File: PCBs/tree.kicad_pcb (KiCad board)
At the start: 2 copper layers, 31 parts, among them J1 Conn_01x06_Female, SW1 SW_Push_DPDT, SW2 SW_SPST, U1 Shift_Reg, U2 Shift_Reg, U3 Shift_Reg, U4 pic18f45k20

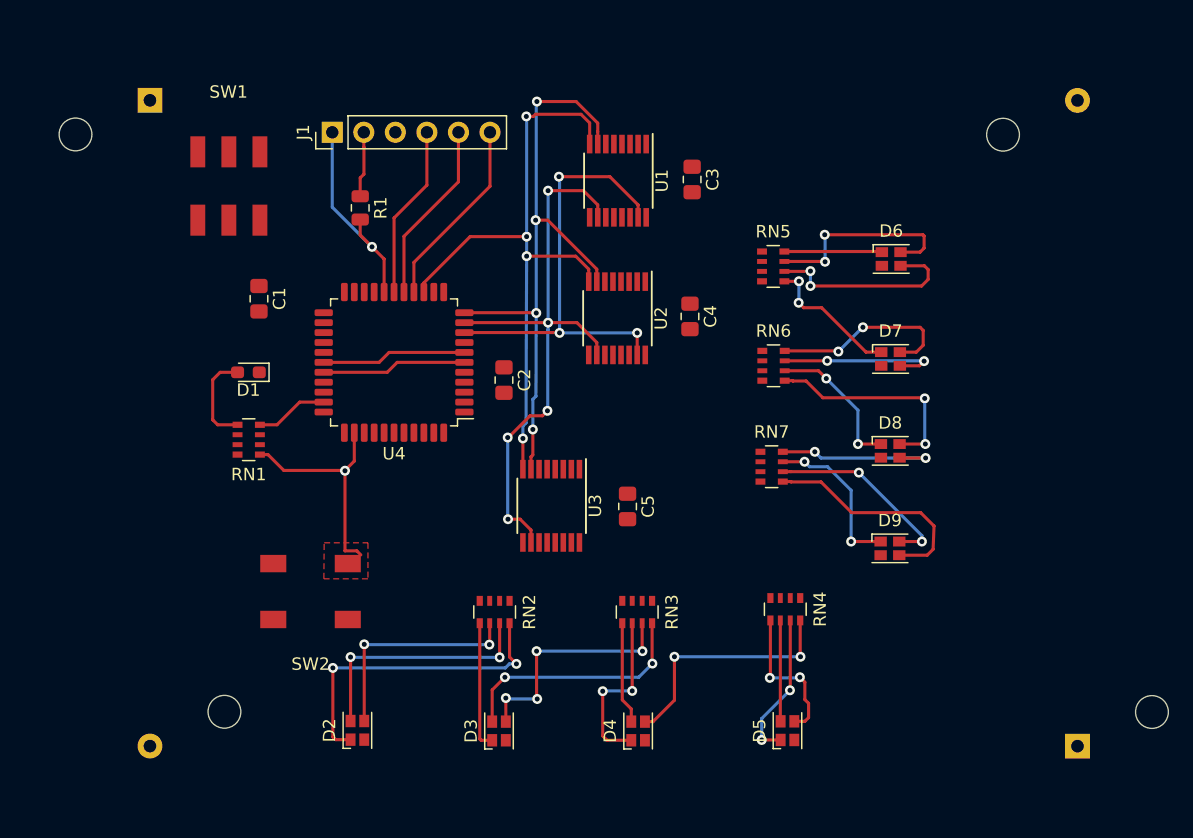
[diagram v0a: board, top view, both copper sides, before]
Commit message: Finished Bulk of routing. Reformated traces to use 6/6 mils as per board house rules.
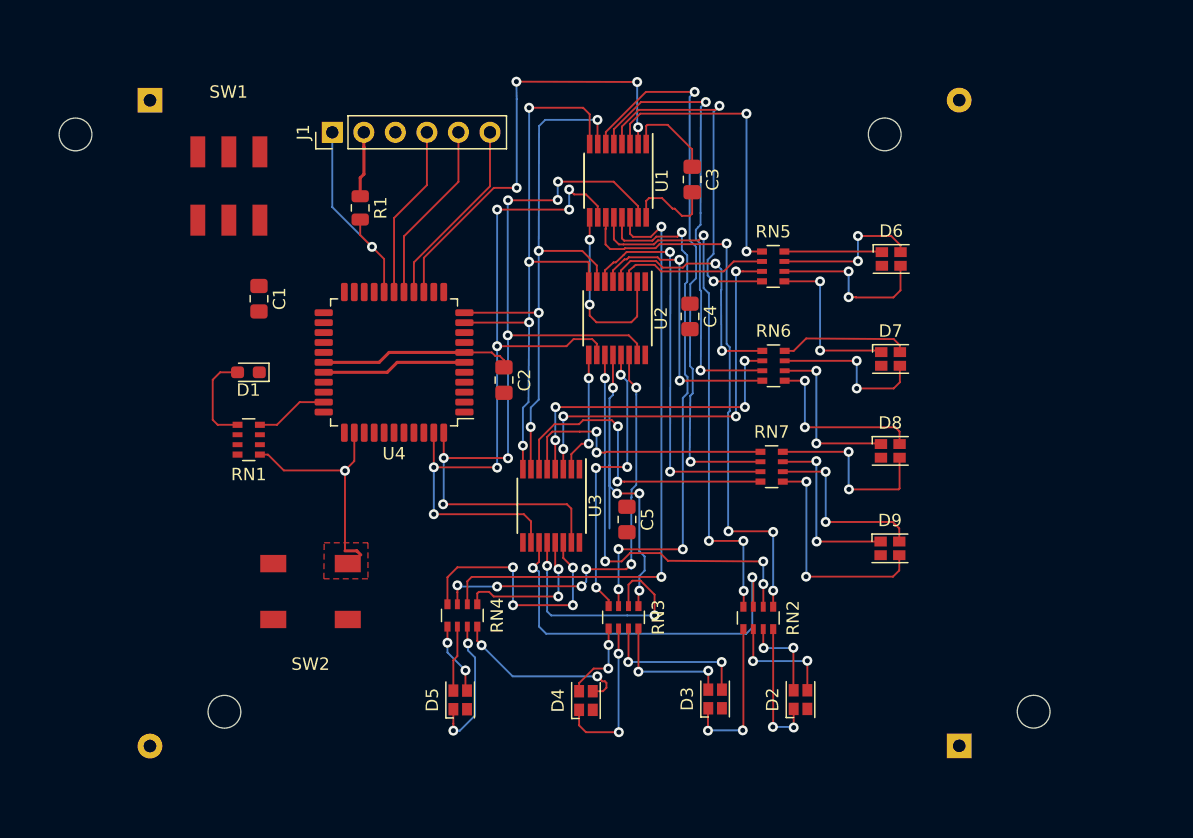
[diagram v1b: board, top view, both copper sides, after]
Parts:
- moved D2 35.8 mm to (212.1, 122.7)
- moved D5 26.5 mm to (184.7, 122.7)
- moved RN4 26.0 mm to (184.8, 115.9)
- moved RN2 21.2 mm to (208.7, 116.1)
- moved D3 17.6 mm to (205.2, 122.6)
- moved BT2 9.53 mm to (224.8, 126.4)
- moved D4 4.86 mm to (194.8, 122.7)
- moved RN3 1.18 mm to (197.8, 116.0)
- moved C5 1.05 mm to (198.1, 108.2)
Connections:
- U4 pad 10: Storage_CLK -> ~Output_Enable~
- U4 pad 14: ~Output_Enable~ -> Red_Data
- U4 pad 43: Net-(U4-Pad43) -> Storage_CLK
- U4 pad 44: Net-(U4-Pad44) -> Shift_CLK
- U4 pad 8: Red_Data -> Net-(U4-Pad8)
- U4 pad 9: Shift_CLK -> Net-(U4-Pad9)
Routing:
- net R8: track 0.00 -> 50.1 mm, vias 0 -> 2
- net R4: track 0.00 -> 46.1 mm, vias 0 -> 2
- net R5: track 0.00 -> 45.3 mm, vias 0 -> 4
- net R7: track 0.00 -> 42.7 mm, vias 0 -> 4
- net R6: track 0.00 -> 42.3 mm, vias 0 -> 4
- net R3: track 0.00 -> 36.6 mm, vias 0 -> 2
- net Red_Data: track 0.00 -> 35.9 mm, vias 0 -> 4
- net G8: track 0.00 -> 34.6 mm, vias 0 -> 6
- net Shift_CLK: track 36.6 -> 70.2 mm, vias 3 -> 7
- net G5: track 0.00 -> 33.5 mm, vias 0 -> 4
- net B1: track 0.00 -> 31.9 mm, vias 0 -> 4
- net G4: track 0.00 -> 31.7 mm, vias 0 -> 2
- net B5: track 0.00 -> 31.3 mm, vias 0 -> 2
- net R2: track 0.00 -> 28.6 mm, vias 0 -> 2
- net G6: track 0.00 -> 27.9 mm, vias 0 -> 4
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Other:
- net class Default: clearance 0.2 -> 0.1524; trace_width 0.25 -> 0.1524
- rule trace_clearance: 0.2 -> 0.1524
- rule trace_min: 0.2 -> 0.1524

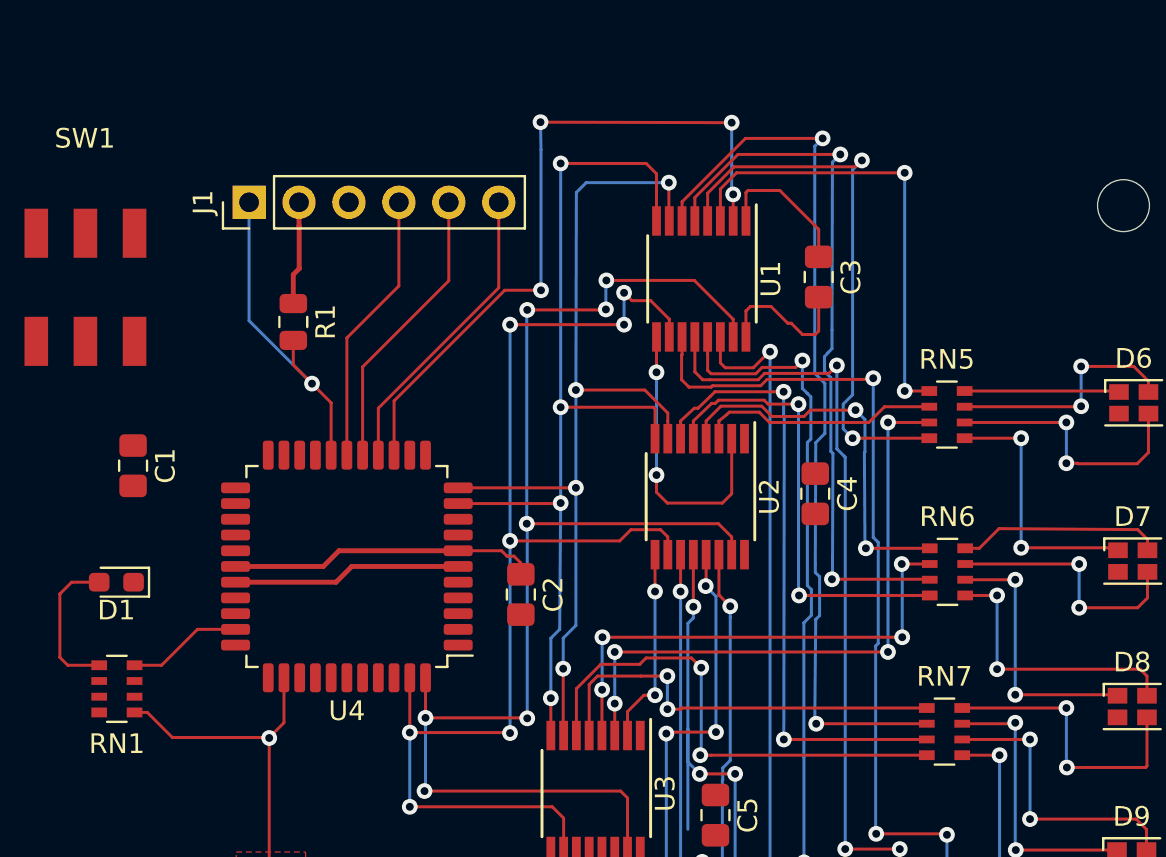
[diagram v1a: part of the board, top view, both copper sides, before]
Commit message: Laid out a board with debug header and LPC804
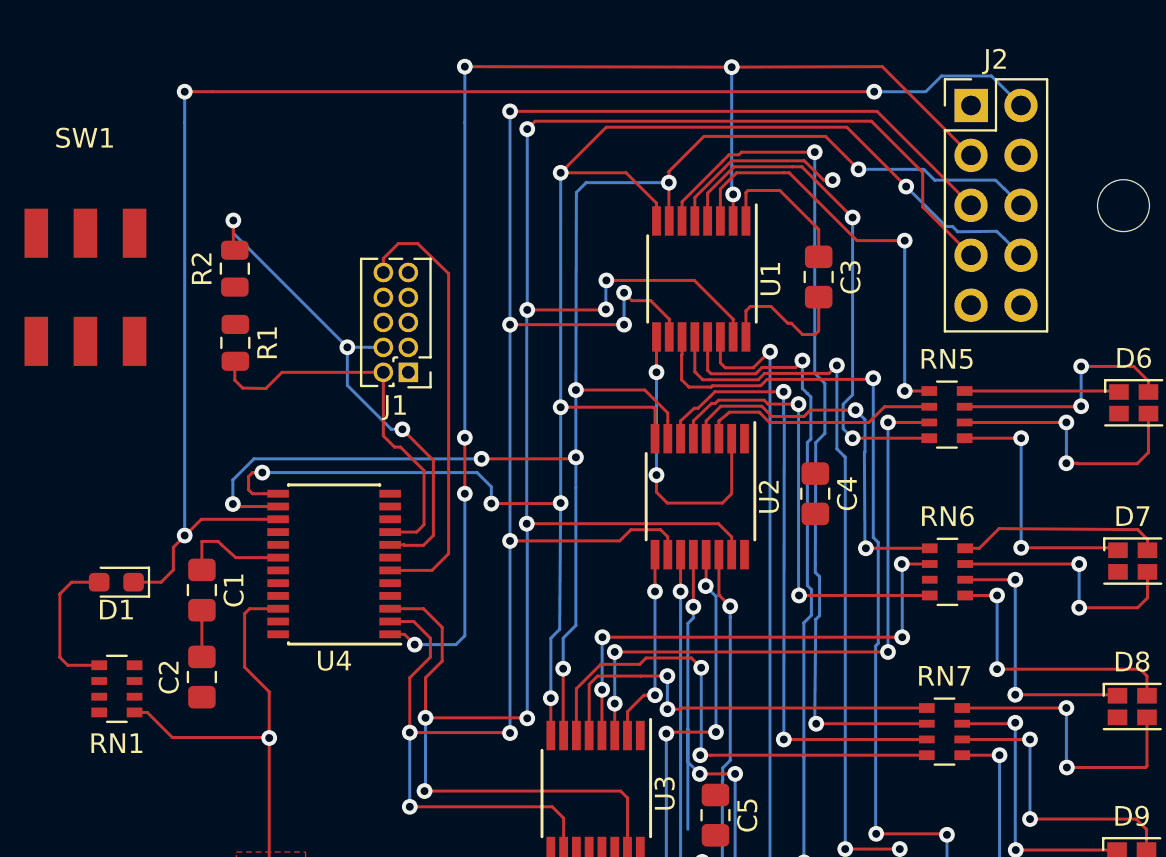
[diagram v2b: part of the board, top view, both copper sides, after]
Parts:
- added J2: Conn_02x05_Odd_Even, Connector_PinHeader_2.54mm:PinHeader_2x05_P2.54mm_Vertical, F.Cu at (211.1, 72.0)
- added R2: 10K, Resistor_SMD:R_0805_2012Metric, F.Cu at (173.6, 80.3)
- J1: value Conn_01x06_Female -> Conn_02x05_Odd_Even; footprint Connector_PinHeader_2.54mm:PinHeader_1x06_P2.54mm_Vertical -> Connector_PinHeader_1.27mm:PinHeader_2x05_P1.27mm_Vertical
- U4: value pic18f45k20 -> LPC804-TSSOP24; footprint Package_QFP:LQFP-44_10x10mm_P0.8mm -> Package_SO:TSSOP-24_4.4x7.8mm_P0.65mm
- moved C2 16.8 mm to (171.9, 101.1), turned to 90 degrees
- moved J1 11.9 mm to (182.4, 85.6), turned to 180 degrees
- moved C1 7.23 mm to (171.9, 96.7)
- moved R1 3.14 mm to (173.7, 84.1)
- moved U4 0.66 mm to (178.7, 95.4)
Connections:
- D1 pad 1: GND -> HB
- J1 pad 1: Net-(J1-Pad1) -> 3v3
- J1 pad 2: 3v3 -> SWDIO_PIO0_2
- J1 pad 4: Net-(J1-Pad4) -> SWCLK_PIO0_3
- J1 pad 5: Net-(J1-Pad5) -> GND
- R1 pad 2: Net-(J1-Pad1) -> SWDIO_PIO0_2
- RN1 pad 4: HB -> 3v3
- U4 pad 1: Net-(U4-Pad1) -> Red_Data
- U4 pad 10: ~Output_Enable~ -> Net-(U4-Pad10)
- U4 pad 11: ~MEM_RESET~ -> Net-(U4-Pad11)
- U4 pad 13: Net-(U4-Pad13) -> ~Output_Enable~
- U4 pad 14: Red_Data -> ~MEM_RESET~
- U4 pad 15: Net-(J1-Pad6) -> HB
- U4 pad 16: Net-(J1-Pad5) -> Net-(U4-Pad16)
- U4 pad 17: Net-(J1-Pad4) -> Net-(U4-Pad17)
- U4 pad 18: Net-(J1-Pad1) -> 3v3
- U4 pad 19: Net-(U4-Pad19) -> GND
- U4 pad 2: Net-(U4-Pad2) -> Storage_CLK
- U4 pad 22: Net-(U4-Pad22) -> BT1
- U4 pad 3: Net-(U4-Pad3) -> Shift_CLK
- U4 pad 6: GND -> !TRST_P0_5
- U4 pad 7: 3v3 -> Net-(U4-Pad7)
- U4 pad 8: Net-(U4-Pad8) -> SWCLK_PIO0_3
- U4 pad 9: Net-(U4-Pad9) -> SWDIO_PIO0_2
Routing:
- net HB: track 5.89 -> 75.4 mm, vias 0 -> 3
- net Shift_CLK: track 70.2 -> 112.0 mm, vias 7 -> 8
- net Storage_CLK: track 63.1 -> 104.2 mm, vias 7 -> 8
- net ~Output_Enable~: track 48.4 -> 88.0 mm, vias 4 -> 7
- net ~MEM_RESET~: track 47.2 -> 83.4 mm, vias 4 -> 7
- net Red_Data: track 35.9 -> 68.6 mm, vias 4 -> 6
- net R3: track 36.6 -> 9.38 mm, vias 2 -> 1
- net SWCLK_PIO0_3: track 0.00 -> 26.4 mm, vias 0 -> 3
- net !TRST_P0_5: track 0.00 -> 22.5 mm
- net SWDIO_PIO0_2: track 0.00 -> 19.7 mm
- net Net-(J1-Pad1): track 17.2 -> 0.00 mm, vias 1 -> 0
- net Net-(J1-Pad6): track 15.4 -> 0.00 mm
- net 3v3: track 28.4 -> 13.1 mm
- net Net-(J1-Pad5): track 14.7 -> 0.00 mm
- net Net-(J1-Pad4): track 14.0 -> 0.00 mm
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
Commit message: Finished Layout, generated gerbers
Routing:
- net Net-(BT1-Pad2): track 0.00 -> 66.7 mm
- net R3: track 9.38 -> 35.0 mm, vias 1 -> 2
- net GND: track 9.88 -> 28.3 mm, vias 0 -> 7
- net 3v3: track 13.1 -> 25.5 mm
- net Net-(BT1-Pad1): track 0.00 -> 9.71 mm
- net G6: track 27.9 -> 22.8 mm
- net !TRST_P0_5: track 22.5 -> 23.4 mm, vias 0 -> 2
- net HB: track 75.4 -> 76.0 mm
- net Net-(D1-Pad2): track 7.64 -> 7.32 mm, vias 0 -> 2
- added copper zone on F.Cu, net 3v3
- added copper zone on B.Cu, net GND
- removed copper zone on F.Cu, net BT1
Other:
- board outline added: 82.5 x 60.7 mm
- board text added: "1"
- board text added: "GND ->"
- board text added: "HB"
- board text added: "Off"
- board text added: "On"
